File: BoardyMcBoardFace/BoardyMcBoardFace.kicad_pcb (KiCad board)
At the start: 4 copper layers, 95 x 24 mm, 83 parts, among them J1 SMA, J2 ARM 10pin, J3 USB_B_Micro, SW1 SW_Push, U1 nRF24L01P, U2 STM32F103CBT6, U3 USBLC6-2SC6, U4 LM393, U5 AMS1117-5.0, U6 AMS1117-3.3, U7 USBLC6-2SC6, U8 USBLC6-2SC6, U9 TJA1051T-3, Y1 16MHz, Y2 16MHz

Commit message: fix comments
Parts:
- moved D5 9.24 mm to (189.9, 114.1), turned to 0 degrees
- moved C26 1.40 mm to (197.5, 119.9)
- moved C20 0.97 mm to (191.5, 112.7)
- moved U$1 0.09 mm to (203.4, 110.6)
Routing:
- net Net-(D5-Pad1): track 14.3 -> 4.23 mm
- net /CAN_H: track 17.2 -> 12.8 mm
- net /CAN_L: track 18.6 -> 14.5 mm
- net +5V: track 15.3 -> 18.9 mm
- net /I2C1_SCL: track 23.6 -> 21.6 mm
- net /I2C1_SDA: track 23.3 -> 21.5 mm
- net /USB_CONN_DP: track 4.85 -> 3.28 mm
- net /DRBL_PWM_1: track 37.0 -> 35.5 mm
- net /DRBL_PWM_2: track 36.8 -> 35.3 mm
- net /NRST: track 37.8 -> 36.8 mm
- net +3V3: track 75.4 -> 74.9 mm, vias 36 -> 35
- added copper zone on B.Cu, net GND
- added copper zone on F.Cu, net GND
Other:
- outline, holes or cut-outs redrawn

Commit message: wip
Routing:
- net unconnected-(J3-Pad6): track 12.6 -> 0.00 mm
- net VBUS: track 22.9 -> 23.6 mm

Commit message: wip
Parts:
- moved L2 0.13 mm to (120.9, 107.4)
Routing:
- net GND: track 162.4 -> 163.1 mm

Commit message: wip
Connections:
- J3 pad 6: unconnected-(J3-Pad6) -> GND
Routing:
- net GND: track 163.1 -> 168.3 mm

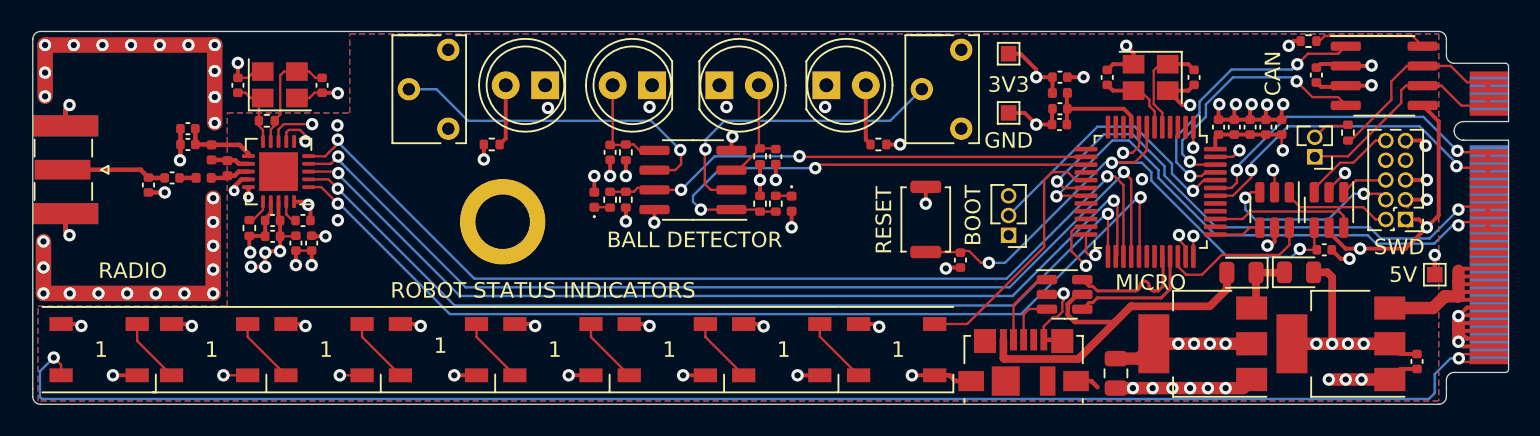
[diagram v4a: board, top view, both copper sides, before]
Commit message: changing to 2020 from 5050 neopixel changed everything
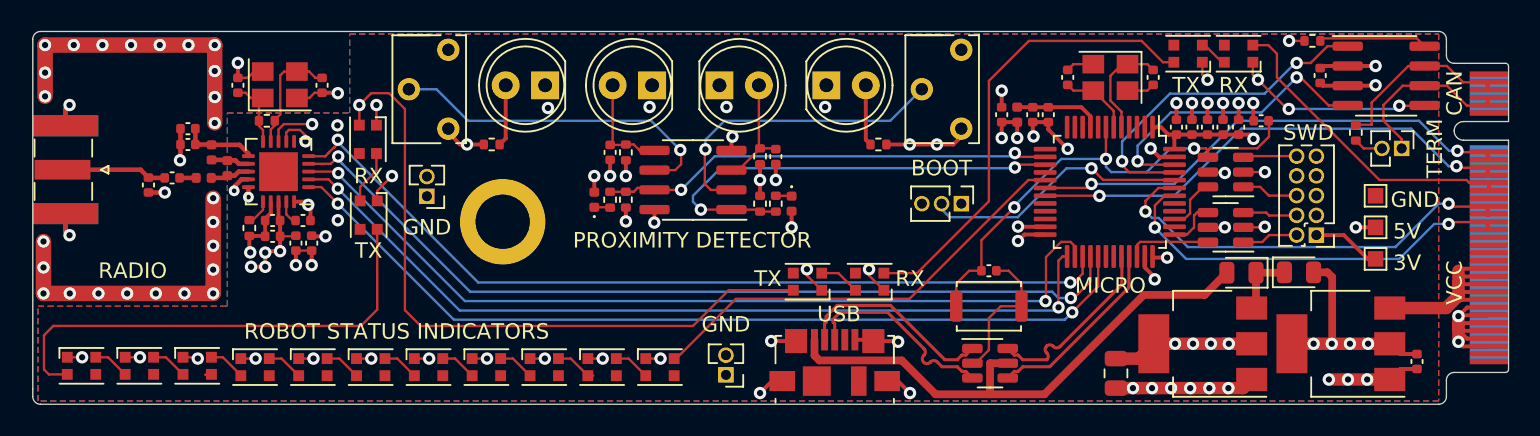
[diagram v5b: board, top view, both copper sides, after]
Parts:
- added D1: WS2812B, LED_SMD:LED_WS2812B-2020_PLCC4_2.0x2.0mm, F.Cu at (130.1, 120.2)
- added D19: WS2812B, LED_SMD:LED_WS2812B-2020_PLCC4_2.0x2.0mm, F.Cu at (122.7, 120.2)
- added D21: WS2812B, LED_SMD:LED_WS2812B-2020_PLCC4_2.0x2.0mm, F.Cu at (186.0, 100.1)
- added D22: WS2812B, LED_SMD:LED_WS2812B-2020_PLCC4_2.0x2.0mm, F.Cu at (182.8, 100.1)
- added D23: WS2812B, LED_SMD:LED_WS2812B-2020_PLCC4_2.0x2.0mm, F.Cu at (162.2, 114.8)
- added D24: WS2812B, LED_SMD:LED_WS2812B-2020_PLCC4_2.0x2.0mm, F.Cu at (158.2, 114.8)
- added D25: WS2812B, LED_SMD:LED_WS2812B-2020_PLCC4_2.0x2.0mm, F.Cu at (129.9, 105.6)
- added D26: WS2812B, LED_SMD:LED_WS2812B-2020_PLCC4_2.0x2.0mm, F.Cu at (130.0, 110.5)
- added D7: WS2812B, LED_SMD:LED_WS2812B-2020_PLCC4_2.0x2.0mm, F.Cu at (126.4, 120.2)
- added J4: Conn_01x02_Male, Connector_PinHeader_1.27mm:PinHeader_1x02_P1.27mm_Vertical, F.Cu at (153.0, 120.8)
- added J5: Conn_01x02_Male, Connector_PinHeader_1.27mm:PinHeader_1x02_P1.27mm_Vertical, F.Cu at (133.8, 109.2)
- D11, D12, D13, D14, D15, D16, D17, D18: footprint LED_SMD:LED_WS2812B_PLCC4_5.0x5.0mm_P3.2mm -> LED_SMD:LED_WS2812B-2020_PLCC4_2.0x2.0mm
- moved TP1 27.1 mm to (194.8, 113.3)
- moved TP4 24.2 mm to (194.8, 109.2), turned to 180 degrees
- moved D11 15.3 mm to (148.7, 120.2)
- moved J3 12.2 mm to (160.0, 119.9)
- moved D12 11.6 mm to (145.0, 120.2)
- moved C20 9.25 mm to (187.5, 104.4), turned to 180 degrees
- moved D16 8.23 mm to (119.0, 120.2)
- moved D13 8.00 mm to (141.3, 120.2)
- moved U7 7.09 mm to (185.2, 107.7), turned to 180 degrees
- moved SW1 6.91 mm to (169.9, 116.3), turned to 180 degrees
- moved U8 6.53 mm to (170.0, 120.0)
- moved J2 5.83 mm to (191.0, 111.8)
- moved JP1 5.62 mm to (196.5, 106.2), turned to -90 degrees
- moved TP3 4.88 mm to (194.8, 111.3)
- moved D17 4.64 mm to (115.2, 120.2)
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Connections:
- D15 pad 2: Net-(D15-Pad2) -> Net-(D1-Pad4)
- D16 pad 4: Net-(D15-Pad2) -> Net-(D16-Pad4)
- D18 pad 2: /PIXEL_OFFBOARD -> Net-(D18-Pad2)
- U$1 pad P$21: /I2C1_SDA -> /DRBL_PWM_1
- U$1 pad P$23: /I2C1_SDA -> /DRBL_PWM_1
- U$1 pad P$25: /I2C1_SCL -> /DRBL_PWM_2
- U$1 pad P$27: /I2C1_SCL -> /DRBL_PWM_2
- U$1 pad P$29: unconnected-(U$1-PadP$29) -> /PIXEL_OFFBOARD
- U$1 pad P$31: unconnected-(U$1-PadP$31) -> /PIXEL_OFFBOARD
- U$1 pad P$35: /DRBL_PWM_1 -> /I2C1_SDA
- U$1 pad P$37: /DRBL_PWM_1 -> /I2C1_SDA
- U$1 pad P$39: /DRBL_PWM_2 -> /I2C1_SCL
- U$1 pad P$41: /DRBL_PWM_2 -> /I2C1_SCL
- U$1 pad P$73: /PIXEL_OFFBOARD -> unconnected-(U$1-PadP$73)
- U$1 pad P$75: /PIXEL_OFFBOARD -> unconnected-(U$1-PadP$75)
- U2 pad 10: /STRAIN_ADC1_0 -> unconnected-(U2-Pad10)
- U2 pad 11: /STRAIN_ADC1_1 -> unconnected-(U2-Pad11)
- U2 pad 12: /STRAIN_ADC1_2 -> unconnected-(U2-Pad12)
- U2 pad 13: /STRAIN_ADC1_3 -> unconnected-(U2-Pad13)
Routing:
- net /PIXEL_OFFBOARD: track 101.4 -> 20.3 mm, vias 2 -> 0
- net Net-(D24-Pad4): track 0.00 -> 44.3 mm, vias 0 -> 1
- net Net-(D18-Pad2): track 0.00 -> 31.1 mm
- net Net-(D22-Pad4): track 0.00 -> 30.0 mm
- net GND: track 168.3 -> 144.4 mm, vias 90 -> 77
- net +3V3: track 74.9 -> 87.9 mm, vias 35 -> 46
- net /PIXEL_MOSI: track 15.8 -> 28.7 mm
- net VBUS: track 23.6 -> 35.0 mm
- net /USB_CONN_DP: track 3.28 -> 13.0 mm
- net /RADIO_SPI_MISO: track 64.5 -> 55.7 mm
- net /RADIO_SPI_MOSI: track 65.0 -> 56.5 mm
- net /SWCLK_CONN: track 12.0 -> 3.52 mm, vias 2 -> 0
- net /USB_CONN_DN: track 5.07 -> 13.0 mm
- net /RADIO_CE: track 63.9 -> 57.2 mm
- net /I2C1_SDA: track 21.5 -> 27.6 mm
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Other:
- board text added: "3V"
- board text added: "PROXIMITY DETECTOR"
- board text added: "RX"
- board text added: "TERM"
- board text added: "TX"
- board text added: "USB"
- board text added: "VCC"
- board text removed: "3V3"
- board text removed: "BALL DETECTOR"
- board text removed: "DESIGNED BY AKHIL V"
- board text removed: "RESET"

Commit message: finishing touches again??
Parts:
- added C28: 100n, Capacitor_SMD:C_0402_1005Metric, F.Cu at (185.8, 102.1)
- added C31: 100n, Capacitor_SMD:C_0402_1005Metric, F.Cu at (182.6, 102.1)
- added C32: 100n, Capacitor_SMD:C_0402_1005Metric, F.Cu at (133.5, 118.4)
- added C33: 100n, Capacitor_SMD:C_0402_1005Metric, F.Cu at (157.7, 112.9)
- added C34: 100n, Capacitor_SMD:C_0402_1005Metric, F.Cu at (114.8, 118.4)
- added C35: 100n, Capacitor_SMD:C_0402_1005Metric, F.Cu at (130.1, 103.5)
- added C36: 100n, Capacitor_SMD:C_0402_1005Metric, F.Cu at (111.1, 118.4)
- added C37: 100n, Capacitor_SMD:C_0402_1005Metric, F.Cu at (148.3, 118.4)
- added C38: 100n, Capacitor_SMD:C_0402_1005Metric, F.Cu at (129.8, 118.4)
- added C39: 100n, Capacitor_SMD:C_0402_1005Metric, F.Cu at (137.2, 118.4)
- added C40: 100n, Capacitor_SMD:C_0402_1005Metric, F.Cu at (140.9, 118.4)
- added C41: 100n, Capacitor_SMD:C_0402_1005Metric, F.Cu at (122.3, 118.4)
- added C42: 100n, Capacitor_SMD:C_0402_1005Metric, F.Cu at (144.6, 118.4)
- added C43: 100n, Capacitor_SMD:C_0402_1005Metric, F.Cu at (118.6, 118.4)
- added C44: 100n, Capacitor_SMD:C_0402_1005Metric, F.Cu at (126.0, 118.4)
- added C45: 100n, Capacitor_SMD:C_0402_1005Metric, F.Cu at (161.0, 112.9)
- added C46: 100n, Capacitor_SMD:C_0402_1005Metric, F.Cu at (127.8, 112.7)
- moved J5 39.6 mm to (172.6, 101.6)
- moved JP2 0.76 mm to (168.2, 110.5)
- moved D23 0.65 mm to (161.6, 114.8)
- moved R3 0.44 mm to (193.5, 105.6)
- moved D21 0.22 mm to (186.0, 100.3)
- moved D22 0.22 mm to (182.8, 100.3)
- moved D16 0.08 mm to (119.0, 120.2)
- moved D17 0.08 mm to (115.2, 120.2)
- moved D18 0.08 mm to (111.5, 120.2)
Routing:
- net GND: track 144.4 -> 212.0 mm, vias 77 -> 102
- net +3V3: track 87.9 -> 109.9 mm, vias 46 -> 47
- net Net-(D24-Pad4): track 44.3 -> 40.0 mm, vias 1 -> 0
- net Net-(D22-Pad4): track 30.0 -> 27.8 mm, vias 0 -> 2
- net /NRST: track 31.8 -> 33.2 mm
- net /CAN_RX: track 19.6 -> 18.6 mm
- net /CAN_TX: track 22.2 -> 21.4 mm
- net /DRBL_PWM_2: track 31.8 -> 31.2 mm
- net Net-(D23-Pad4): track 2.63 -> 1.98 mm
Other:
- board text added: "DETECTOR"
- board text removed: "PROXIMITY DETECTOR"

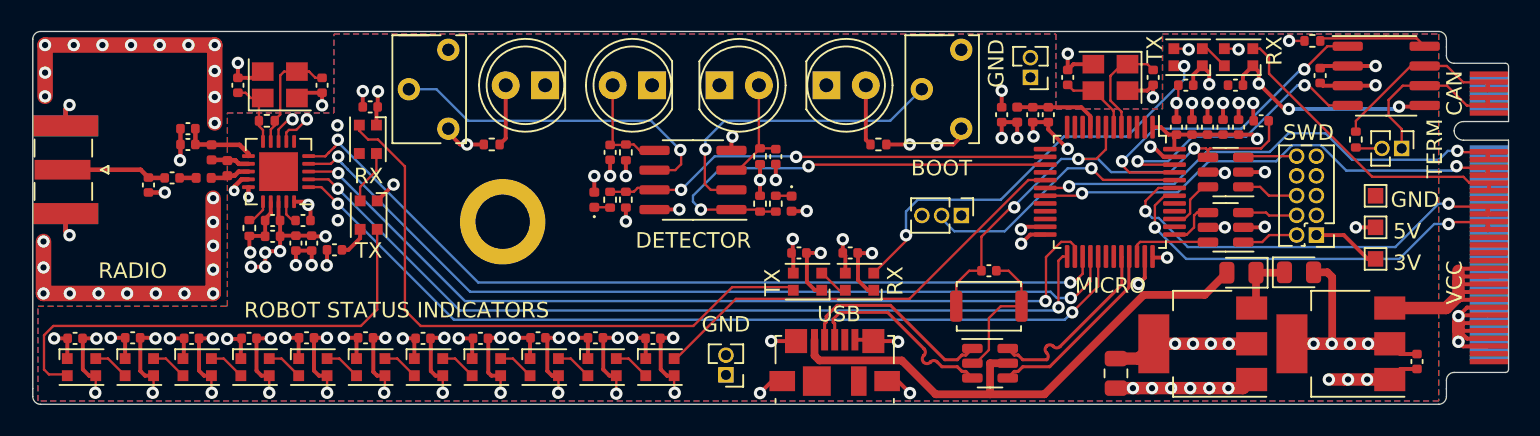
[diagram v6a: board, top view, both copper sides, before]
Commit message: actually final touches, ground plane ontop looks weird
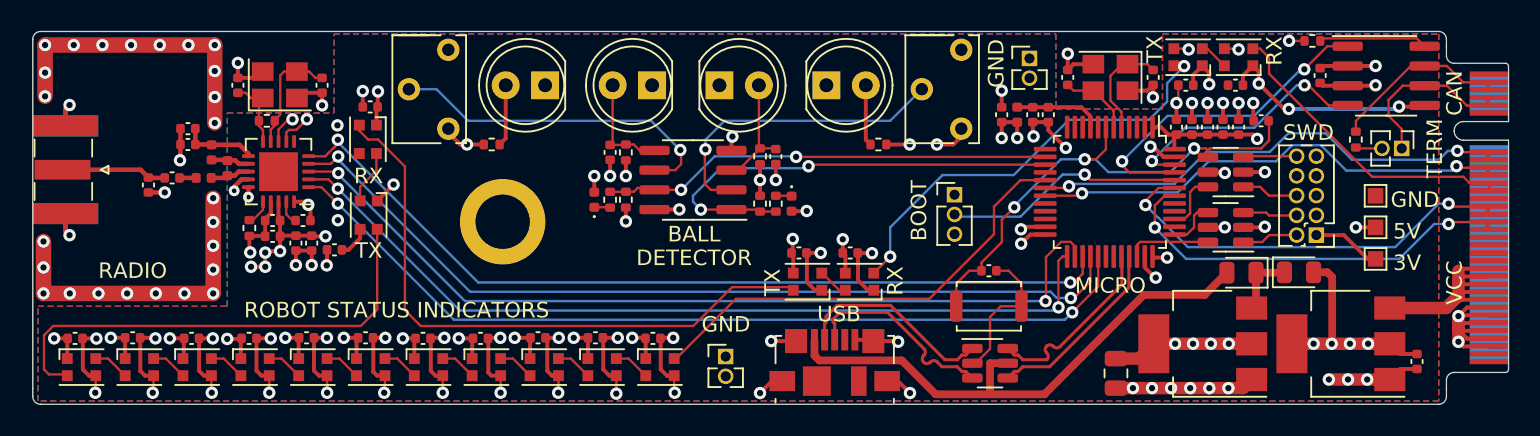
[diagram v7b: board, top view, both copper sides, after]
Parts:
- moved JP2 1.41 mm to (167.7, 109.2), turned to 0 degrees
- moved J5 1.22 mm to (172.5, 100.4), turned to 0 degrees
- moved J4 1.18 mm to (153.0, 119.6), turned to 0 degrees
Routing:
- net /BOOT: track 17.5 -> 15.5 mm
- net /CAN_RX: track 18.6 -> 16.7 mm
- net /PIXEL_MOSI: track 28.5 -> 29.6 mm
- net GND: track 212.0 -> 211.1 mm
- net /NRST: track 33.2 -> 32.6 mm
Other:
- board text added: "BALL"
